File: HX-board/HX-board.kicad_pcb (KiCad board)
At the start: 2 copper layers, 63.5 x 63.9 mm, 101 parts, among them J1 Testpoints, J2 PCIE-LP-01-01-F-DV-A-TR, J3 DB15_Female, J4 Testpoints, J5 DB15_Female, Q1 MMBT4403LT3G, Q2 MMBT4403LT3G, Q3 MMBT4403LT3G, Q4 MMBT4403LT3G, Q5 MMBT4403LT3G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

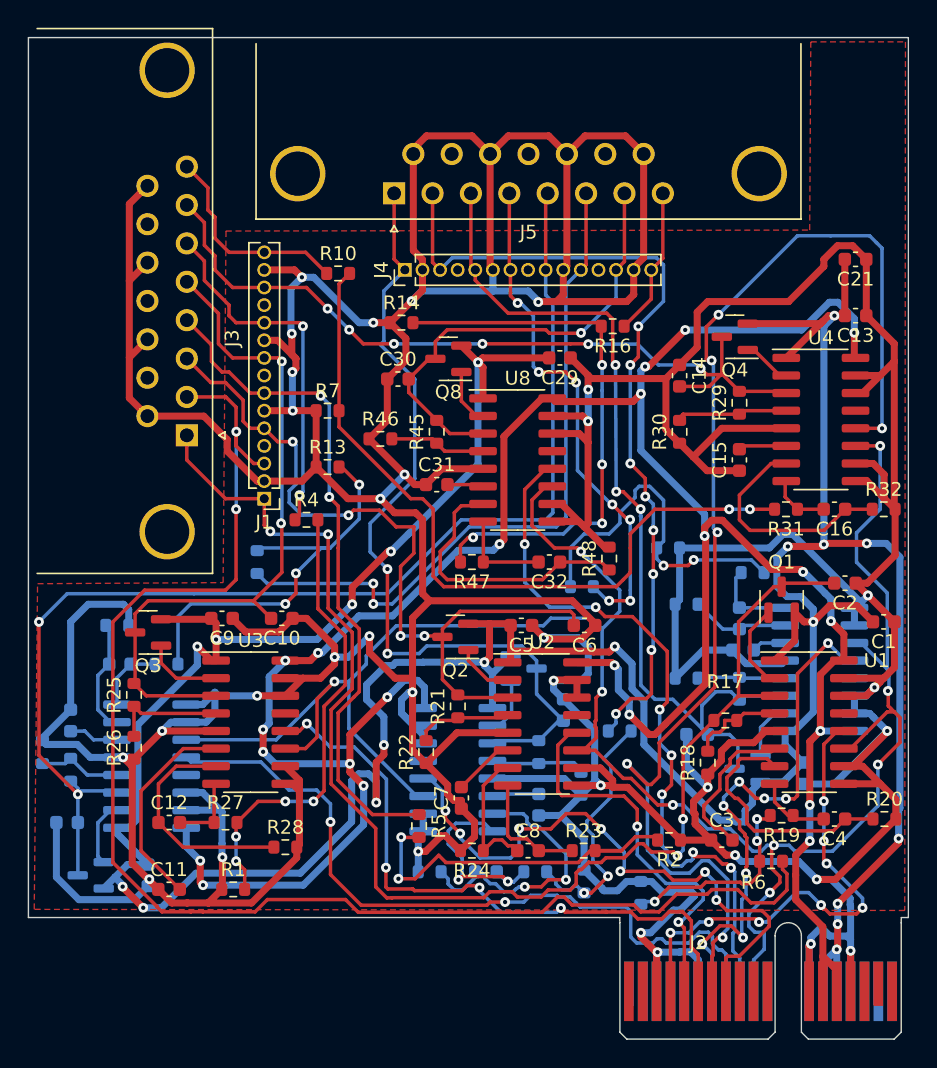
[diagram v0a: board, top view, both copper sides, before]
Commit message: HX Board
Forgot to put GND screen on back
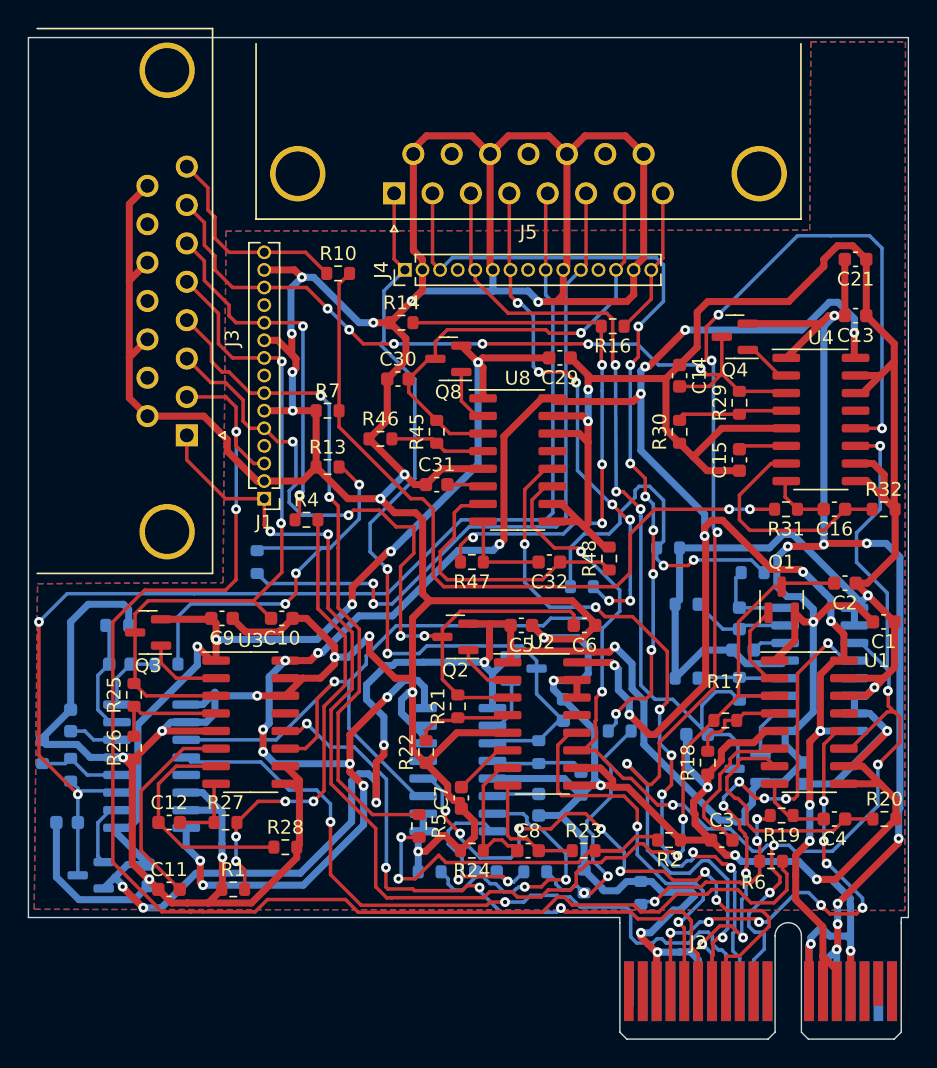
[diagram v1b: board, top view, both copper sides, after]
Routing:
- added copper zone on B.Cu, net GND
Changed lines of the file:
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@@
   (segment (start 127.825 92.456) (end 130.747 92.456) (width 0.254) (layer "F.Cu") (net 111))
   (segment (start 131.636 93.345) (end 134.406 93.345) (width 0.254) (layer "F.Cu") (net 111))
-  (zone (net 1) (net_name "GND") (layer "F.Cu") (hatch edge 0.5)
+  (zone (net 1) (net_name "GND") (layers "F&B.Cu") (hatch edge 0.5)
     (connect_pads (clearance 0.508))
     (min_thickness 0.25) (filled_areas_thickness no)
